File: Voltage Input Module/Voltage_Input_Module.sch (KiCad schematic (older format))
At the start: 21 parts, among them J1 0039281023, J10 0039288060, J11 0039288060, J12 0039288060, J13 0039288060, J14 0039288060, J15 0039288060, J16 0039288060, J17 0039288060, J18 0039288060, J19 0039281023, J2 0039281023, J20 0039281023, J3 0039288060, J4 0039288060, J5 0039288060, J6 0039288060, J7 0039288060, J8 0039288060, J9 0039288060, P1 182-037-113R541

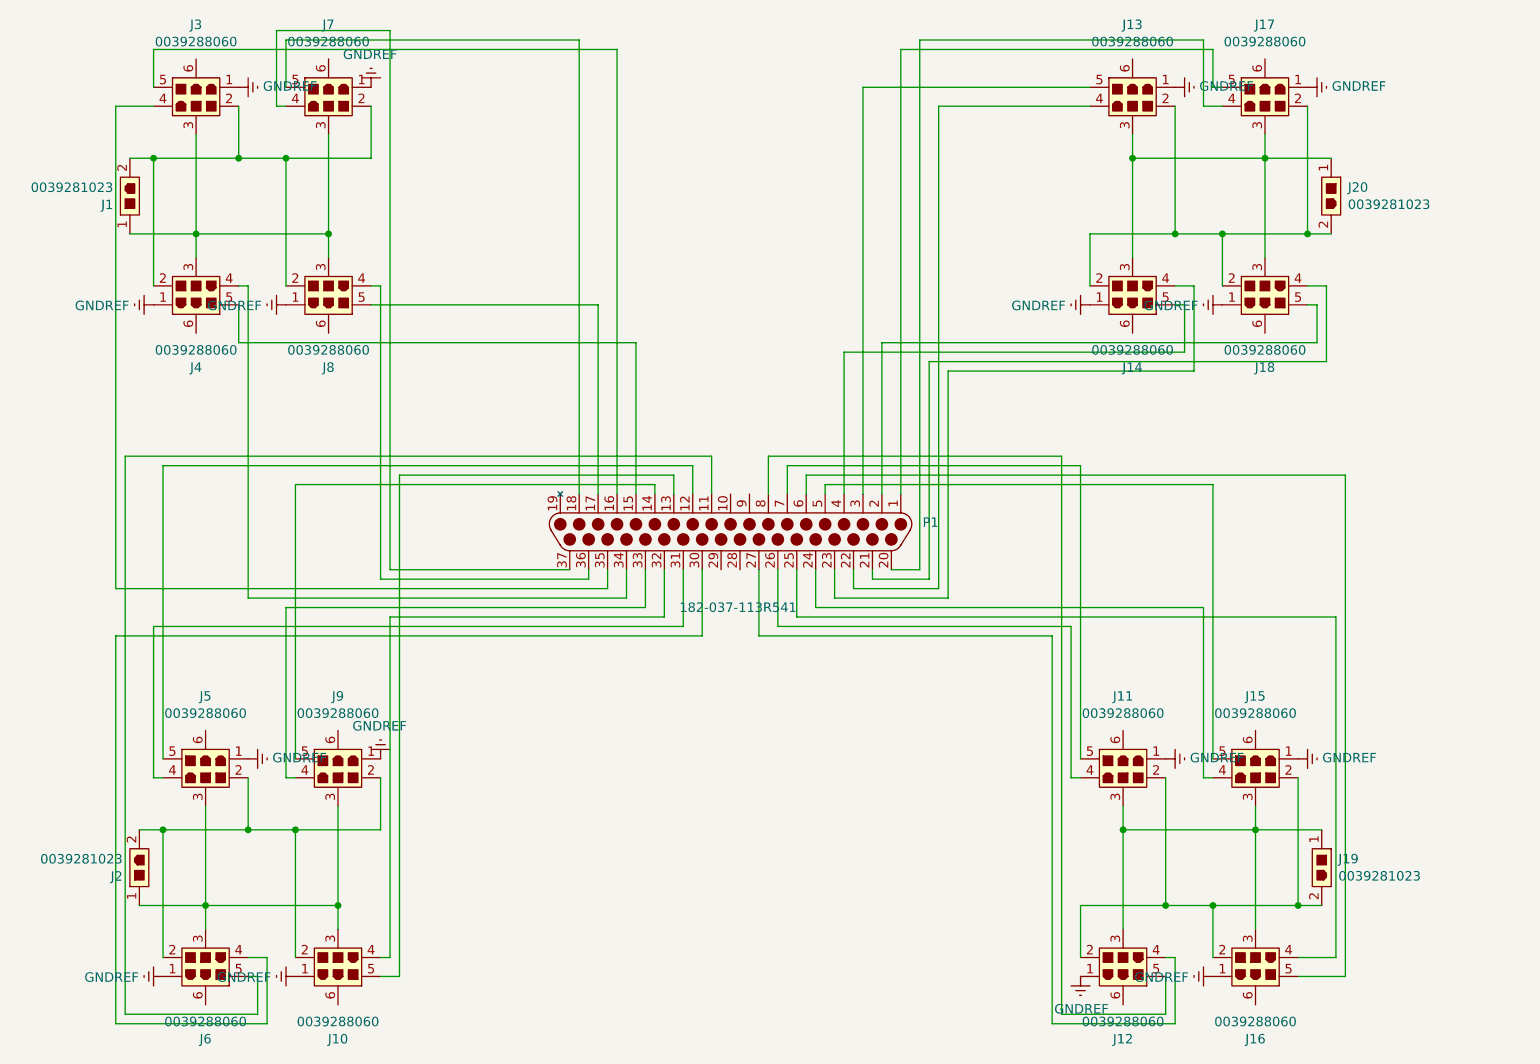
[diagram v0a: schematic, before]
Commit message: Updated Files
Module updates and general fixes
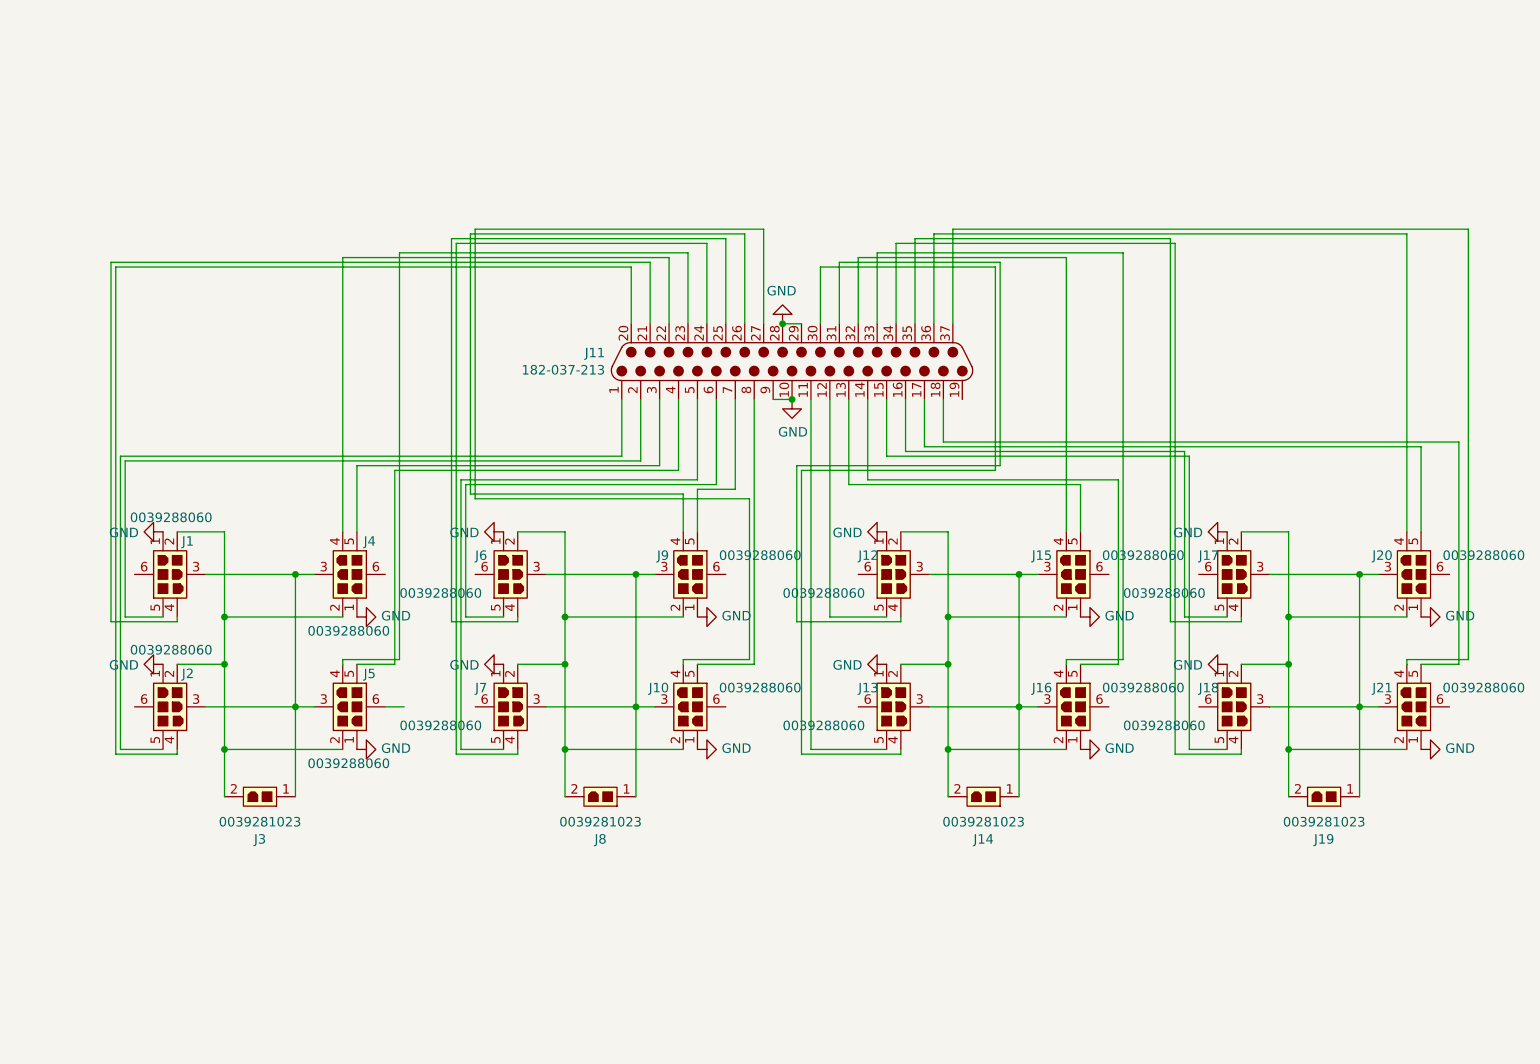
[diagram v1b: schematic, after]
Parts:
- removed J1, J19, J2, J20: 0039281023, Voltage_Input_Module:0039281023, symbol dk_Rectangular-Connectors-Headers-Male-Pins:0039281023
- removed J10, J11, J12, J13, J14, J15, J16, J17, J18, J3, J4, J5, J6, J7, J8, J9: 0039288060, Voltage_Input_Module:0039288060, symbol dk_Rectangular-Connectors-Headers-Male-Pins:0039288060
- removed P1: 182-037-113R541, Voltage_Input_Module:182-037-113R451, symbol dk_Rectangular-Connectors-Headers-Male-Pins:182-037-113R541
- added J1, J10, J12, J13, J15, J16, J17, J18, J2, J20, J21, J4, J5, J6, J7, J9: 0039288060, custom-footprint-library:0039288060, symbol custom-symbols:0039288060
- added J11: 182-037-213, custom-footprint-library:182-037-213R181, symbol custom-symbols:182-037-213
- added J14, J19, J3, J8: 0039281023, custom-footprint-library:0039281023, symbol custom-symbols:0039281023
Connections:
- new net: J11.1, J2.5
- new net: J11.11, J13.5
- new net: J11.12, J12.5
- new net: J11.13, J15.5
- new net: J11.14, J16.5
- new net: J11.15, J18.5
- new net: J11.16, J17.5
- new net: J11.17, J20.5
- new net: J11.18, J21.5
- new net: J1.5, J11.2
- new net: J11.20, J2.4
- new net: J1.4, J11.21
- new net: J11.22, J4.4
- new net: J11.23, J5.4
- new net: J11.24, J7.4
- new net: J11.25, J6.4
- new net: J11.26, J9.4
- new net: J10.4, J11.27
- new net: J11.3, J4.5
- new net: J11.30, J13.4
- new net: J11.31, J12.4
- new net: J11.32, J15.4
- new net: J11.33, J16.4
- new net: J11.34, J18.4
- new net: J11.35, J17.4
- new net: J11.36, J20.4
- new net: J11.37, J21.4
- new net: J11.4, J5.5
- new net: J11.5, J7.5
- new net: J11.6, J6.5
- new net: J11.7, J9.5
- new net: J10.5, J11.8
- new net: J10.3, J6.3, J7.3, J8.1, J9.3
- new net: J10.2, J6.2, J7.2, J8.2, J9.2
- new net: J12.3, J13.3, J14.1, J15.3, J16.3
- new net: J12.2, J13.2, J14.2, J15.2, J16.2
- new net: J1.3, J2.3, J3.1, J4.3, J5.3
- new net: J1.2, J2.2, J3.2, J4.2, J5.2
- new net: J17.3, J18.3, J19.1, J20.3, J21.3
- new net: J17.2, J18.2, J19.2, J20.2, J21.2
- new net GND: J1.1, J10.1, J11.10, J11.28, J11.29, J11.9, J12.1, J13.1, J15.1, J16.1, J17.1, J18.1, J2.1, J20.1, J21.1, J4.1, J5.1, J6.1, J7.1, J9.1
